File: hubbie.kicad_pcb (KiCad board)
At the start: 2 copper layers, 96.6 x 67.4 mm, 70 parts, among them J1 USB_B_Micro, J10 MotorAL, J11 MotorAR, J12 SERVO_0, J13 SERVO_1, J14 DEBUG, J15 AIR_SENSOR, J16 RST_BTN, J17 SERIAL, J18 ActionBtn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

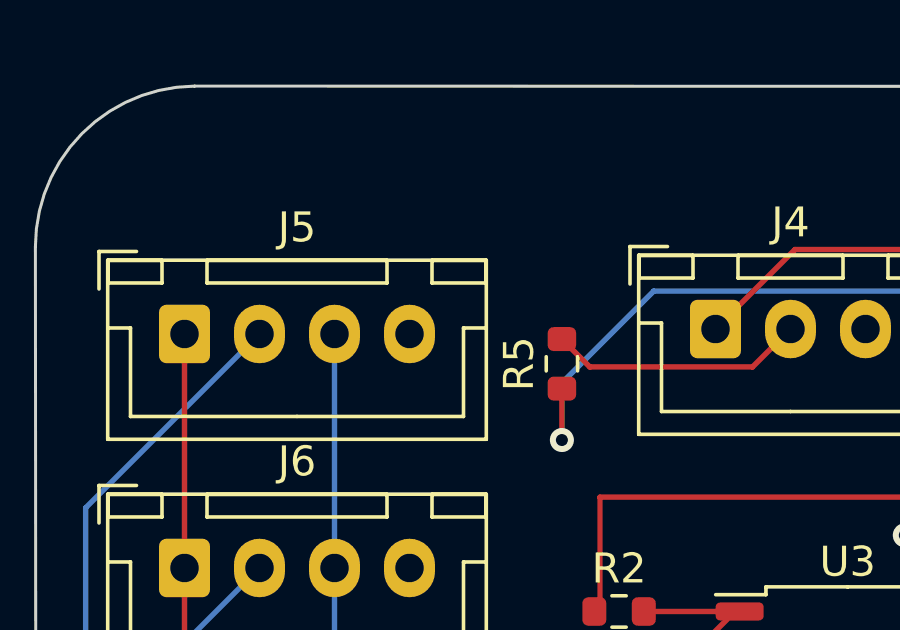
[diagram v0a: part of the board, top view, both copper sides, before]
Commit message: Updated ultrasonic sensor vcc to 5v
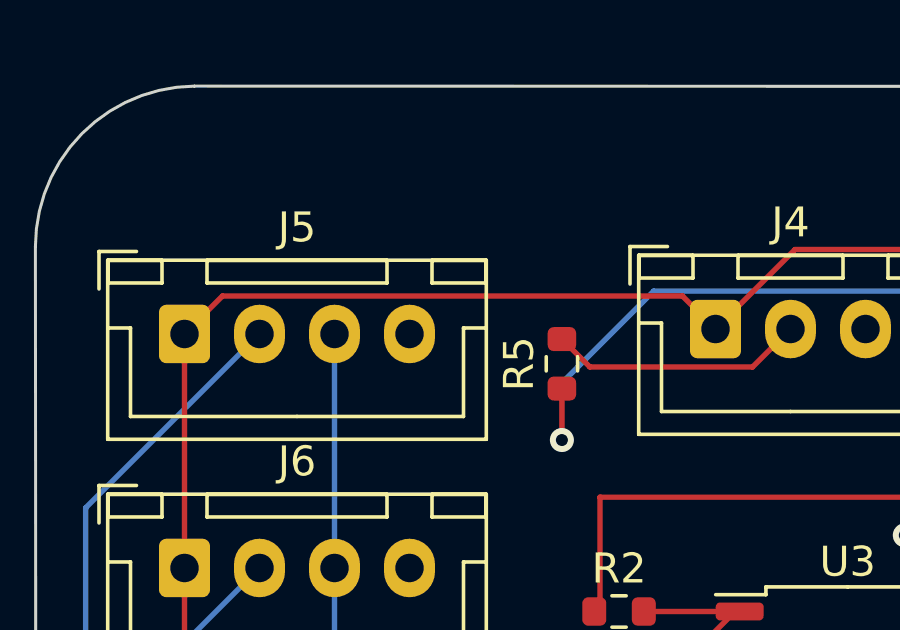
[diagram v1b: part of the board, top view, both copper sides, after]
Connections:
- J5 pad 1: +3.3V -> VBUS
- J6 pad 1: +3.3V -> VBUS
- J7 pad 1: +3.3V -> VBUS
- Y1 pad 2: (no net) -> Net-(C2-Pad2)
- Y1 pad 3: Net-(C2-Pad2) -> (no net)
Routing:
- net VBUS: track 120.9 -> 155.2 mm
- net +3.3V: track 128.1 -> 112.5 mm
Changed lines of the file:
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@@
       (stroke (width 0.1) (type solid)) (layer "F.Fab"))
     (pad "1" thru_hole roundrect (at 0 0) (size 1.7 1.95) (drill 0.95) (layers "*.Cu" "*.Mask") (roundrect_rratio 0.1470588235)
-      (net 7 "+3.3V") (pinfunction "Pin_1") (pintype "passive"))
+      (net 6 "VBUS") (pinfunction "Pin_1") (pintype "passive"))
     (pad "2" thru_hole oval (at 2.5 0) (size 1.7 1.95) (drill 0.95) (layers "*.Cu" "*.Mask")
       (net 20 "/US0") (pinfunction "Pin_2") (pintype "passive"))
@@
       (net 4 "/XIN") (pinfunction "1") (pintype "passive"))
     (pad "2" smd rect (at 1.65 1) (size 1.6 1.3) (layers "F.Cu" "F.Paste" "F.Mask")
-      (pinfunction "2") (pintype "passive"))
-    (pad "3" smd rect (at 1.65 -1) (size 1.6 1.3) (layers "F.Cu" "F.Paste" "F.Mask")
-      (net 5 "Net-(C2-Pad2)"))
+      (net 5 "Net-(C2-Pad2)") (pinfunction "2") (pintype "passive"))
+    (pad "3" smd rect (at 1.65 -1) (size 1.6 1.3) (layers "F.Cu" "F.Paste" "F.Mask"))
     (pad "4" smd rect (at -1.65 -1) (size 1.6 1.3) (layers "F.Cu" "F.Paste" "F.Mask"))
     (model "${KICAD6_3DMODEL_DIR}/Crystal.3dshapes/Crystal_SMD_5032-4Pin_5.0x3.2mm.wrl"
@@
       (stroke (width 0.1) (type solid)) (layer "F.Fab"))
     (pad "1" thru_hole roundrect (at 0 0) (size 1.7 1.95) (drill 0.95) (layers "*.Cu" "*.Mask") (roundrect_rratio 0.1470588235)
-      (net 7 "+3.3V") (pinfunction "Pin_1") (pintype "passive"))
+      (net 6 "VBUS") (pinfunction "Pin_1") (pintype "passive"))
     (pad "2" thru_hole oval (at 2.5 0) (size 1.7 1.95) (drill 0.95) (layers "*.Cu" "*.Mask")
       (net 23 "/US2") (pinfunction "Pin_2") (pintype "passive"))
@@
       (stroke (width 0.1) (type solid)) (layer "F.Fab"))
     (pad "1" thru_hole roundrect (at 0 0) (size 1.7 1.95) (drill 0.95) (layers "*.Cu" "*.Mask") (roundrect_rratio 0.1470588235)
-      (net 7 "+3.3V") (pinfunction "Pin_1") (pintype "passive"))
+      (net 6 "VBUS") (pinfunction "Pin_1") (pintype "passive"))
     (pad "2" thru_hole oval (at 2.5 0) (size 1.7 1.95) (drill 0.95) (layers "*.Cu" "*.Mask")
       (net 22 "/US1") (pinfunction "Pin_2") (pintype "passive"))
@@
   (segment (start 181.47 111.125) (end 179.47 109.125) (width 0.18) (layer "F.Cu") (net 5))
   (segment (start 179.07 109.125) (end 179.07 106.87) (width 0.18) (layer "F.Cu") (net 5))
+  (segment (start 147.435 76.48) (end 162.77 76.48) (width 0.18) (layer "F.Cu") (net 6))
+  (segment (start 146.17 85.545) (end 146.17 77.745) (width 0.18) (layer "F.Cu") (net 6))
+  (segment (start 146.17 85.545) (end 146.17 93.345) (width 0.18) (layer "F.Cu") (net 6))
   (segment (start 166.52 74.93) (end 194.26 74.93) (width 0.18) (layer "F.Cu") (net 6))
   (segment (start 204.965 85.23) (end 205.105 85.09) (width 0.25) (layer "F.Cu") (net 6))
@@
   (segment (start 205.105 85.09) (end 205.74 84.455) (width 0.25) (layer "F.Cu") (net 6))
   (segment (start 194.26 74.93) (end 194.285 74.955) (width 0.18) (layer "F.Cu") (net 6))
+  (segment (start 146.17 77.745) (end 147.435 76.48) (width 0.18) (layer "F.Cu") (net 6))
   (segment (start 205.74 84.455) (end 205.74 73.66) (width 0.25) (layer "F.Cu") (net 6))
+  (segment (start 162.77 76.48) (end 163.87 77.58) (width 0.18) (layer "F.Cu") (net 6))
   (segment (start 194.285 74.955) (end 194.285 84.695) (width 0.18) (layer "F.Cu") (net 6))
   (segment (start 197.585 84.695) (end 194.285 84.695) (width 0.25) (layer "F.Cu") (net 6))
@@
   (segment (start 183.3125 95.4925) (end 182.9125 95.4925) (width 0.18) (layer "F.Cu") (net 7))
   (segment (start 179.883333 100.82) (end 178.8225 100.82) (width 0.18) (layer "F.Cu") (net 7))
-  (segment (start 146.17 85.545) (end 146.17 77.745) (width 0.18) (layer "F.Cu") (net 7))
-  (segment (start 146.17 85.545) (end 146.17 93.345) (width 0.18) (layer "F.Cu") (net 7))
   (segment (start 180.9125 95.4925) (end 181.3125 95.4925) (width 0.18) (layer "F.Cu") (net 7))
   (segment (start 163.035 113.825) (end 162.56 114.3) (width 0.18) (layer "F.Cu") (net 7))

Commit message: Add usb c support and fix wrong voltage sources
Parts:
- removed J1: USB_B_Micro, Connector_USB:USB_Micro-B_Amphenol_10118194_Horizontal
- added J21: DHT22, Connector_JST:JST_XH_B3B-XH-A_1x03_P2.50mm_Vertical, F.Cu at (147.4, 103.0)
- added J22: USB_C_Receptacle_USB2.0, Connector_USB:USB_C_Receptacle_XKB_U262-16XN-4BVC11, F.Cu at (205.1, 71.8)
- added R7: 5.4k, Resistor_SMD:R_0603_1608Metric, F.Cu at (197.7, 74.9)
- added R8: 5.4k, Resistor_SMD:R_0603_1608Metric, F.Cu at (197.7, 71.8)
- J15: footprint Connector_JST:JST_XH_B4B-XH-A_1x04_P2.50mm_Vertical -> Connector_JST:JST_XH_B5B-XH-AM_1x05_P2.50mm_Vertical
- moved H3 11.6 mm to (160.0, 92.1)
- moved H1 1.27 mm to (199.4, 80.0)
- moved C21 0.85 mm to (161.3, 100.3)
- moved C17 0.42 mm to (163.4, 97.2)
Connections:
- U5 pad 41: unconnected-(U5-GPIO29_ADC3-Pad41) -> /DHT
- Y1 pad 2: Net-(C2-Pad2) -> (no net)
- Y1 pad 3: (no net) -> Net-(C2-Pad2)
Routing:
- net /DHT: track 0.00 -> 87.5 mm, vias 0 -> 6
- net GND: track 135.8 -> 162.7 mm, vias 12 -> 14
- net +3.3V: track 112.5 -> 136.6 mm, vias 12 -> 13
- net Net-(J22-CC2): track 0.00 -> 11.9 mm, vias 0 -> 2
- net Net-(J22-CC1): track 0.00 -> 11.3 mm
- net VBUS: track 155.2 -> 164.6 mm
- net /US2: track 47.2 -> 55.7 mm
- net /US0: track 68.1 -> 73.3 mm
- net /US1: track 59.8 -> 64.8 mm
- net /USB_D+: track 32.1 -> 36.9 mm
- net /Jetson_CTL: track 36.8 -> 40.7 mm
- net /SCL: track 111.6 -> 113.8 mm
- net /USB_D-: track 33.0 -> 34.1 mm
- net /RX: track 56.4 -> 57.1 mm
- net /TX: track 52.7 -> 53.5 mm
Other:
- board size 96.6 x 67.4 mm -> 97.1 x 67.9 mm

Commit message: Update wrong capacitor values (C4 and C9)
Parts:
- C4: value 0.1u -> 10n
- C9: value 0.1u -> 22n
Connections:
- Y1 pad 2: (no net) -> Net-(C2-Pad2)
- Y1 pad 3: Net-(C2-Pad2) -> (no net)
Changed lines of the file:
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@@
         (effects (font (size 1 1) (thickness 0.15)))
     )
-    (fp_text value "0.1u" (at 0 1.43 90) (layer "F.Fab")
+    (fp_text value "22n" (at 0 1.43 90) (layer "F.Fab")
         (effects (font (size 1 1) (thickness 0.15)))
     )
@@
       (net 4 "/XIN") (pinfunction "1") (pintype "passive"))
     (pad "2" smd rect (at 1.65 1) (size 1.6 1.3) (layers "F.Cu" "F.Paste" "F.Mask")
-      (pinfunction "2") (pintype "passive"))
-    (pad "3" smd rect (at 1.65 -1) (size 1.6 1.3) (layers "F.Cu" "F.Paste" "F.Mask")
-      (net 5 "Net-(C2-Pad2)"))
+      (net 5 "Net-(C2-Pad2)") (pinfunction "2") (pintype "passive"))
+    (pad "3" smd rect (at 1.65 -1) (size 1.6 1.3) (layers "F.Cu" "F.Paste" "F.Mask"))
     (pad "4" smd rect (at -1.65 -1) (size 1.6 1.3) (layers "F.Cu" "F.Paste" "F.Mask"))
     (model "${KICAD6_3DMODEL_DIR}/Crystal.3dshapes/Crystal_SMD_5032-4Pin_5.0x3.2mm.wrl"
@@
         (effects (font (size 1 1) (thickness 0.15)))
     )
-    (fp_text value "0.1u" (at 0 1.43 90) (layer "F.Fab")
+    (fp_text value "10n" (at 0 1.43 90) (layer "F.Fab")
         (effects (font (size 1 1) (thickness 0.15)))
     )
@@
       (net 14 "/USB_D-") (pinfunction "D-") (pintype "bidirectional"))
     (pad "A8" smd rect (at 1.25 -3.67 180) (size 0.3 1.15) (layers "F.Cu" "F.Paste" "F.Mask")
-      (net 79 "unconnected-(J22-SBU1-PadA8)") (pinfunction "SBU1") (pintype "bidirectional"))
+      (net 79 "unconnected-(J22-SBU1-PadA8)") (pinfunction "SBU1") (pintype "bidirectional+no_connect"))
     (pad "A9" smd rect (at 2.55 -3.67 180) (size 0.3 1.15) (layers "F.Cu" "F.Paste" "F.Mask")
       (net 6 "VBUS") (pinfunction "VBUS") (pintype "passive"))
@@
       (net 14 "/USB_D-") (pinfunction "D-") (pintype "bidirectional"))
     (pad "B8" smd rect (at -1.75 -3.67 180) (size 0.3 1.15) (layers "F.Cu" "F.Paste" "F.Mask")
-      (net 81 "unconnected-(J22-SBU2-PadB8)") (pinfunction "SBU2") (pintype "bidirectional"))
+      (net 81 "unconnected-(J22-SBU2-PadB8)") (pinfunction "SBU2") (pintype "bidirectional+no_connect"))
     (pad "B9" smd rect (at -2.25 -3.67 180) (size 0.3 1.15) (layers "F.Cu" "F.Paste" "F.Mask")
       (net 6 "VBUS") (pinfunction "VBUS") (pintype "passive"))
